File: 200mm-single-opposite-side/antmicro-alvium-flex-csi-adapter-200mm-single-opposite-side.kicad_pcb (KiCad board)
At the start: 2 copper layers, 25.5 x 200.1 mm, 2 parts, among them J1 WE_687622100002_FLEX, J2 WE_687650100002_FLEX

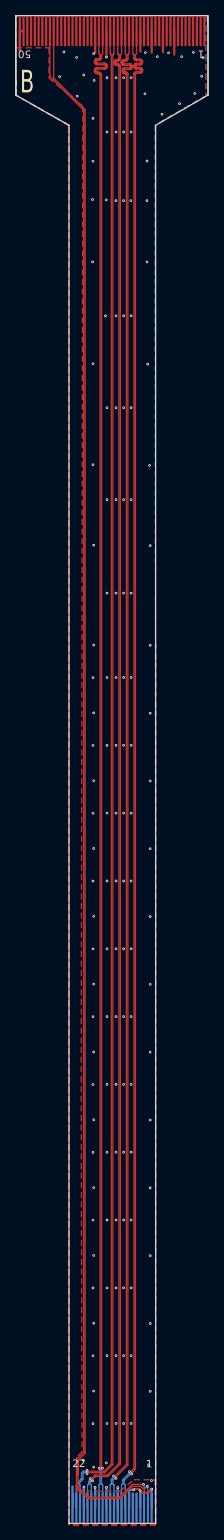
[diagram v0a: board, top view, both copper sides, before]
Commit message: 200mm-single-opposite: update signage
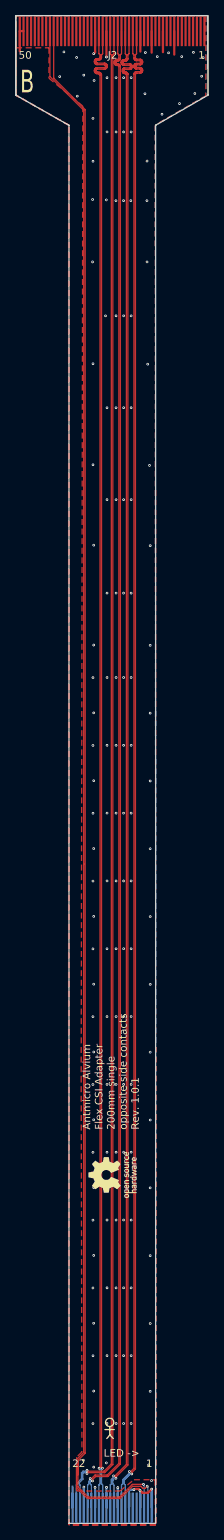
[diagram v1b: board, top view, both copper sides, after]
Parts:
- added N1: oshw_logo, antmicro-alvium-flex-csi-adapter-footprints:oshw-logo, F.Cu at (188.8, 218.6)
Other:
- board text added: "Antmicro Alvium Flex CSI Adapter 200mm single opposite side contacts Rev. 1.0.1"
- board text added: "LED ->"

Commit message: Remove obsolete markings
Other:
- board text removed: "B"
